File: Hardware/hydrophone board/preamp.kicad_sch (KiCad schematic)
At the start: 10 parts, among them J5 Conn_01x02, U111 AD8541ARTZ

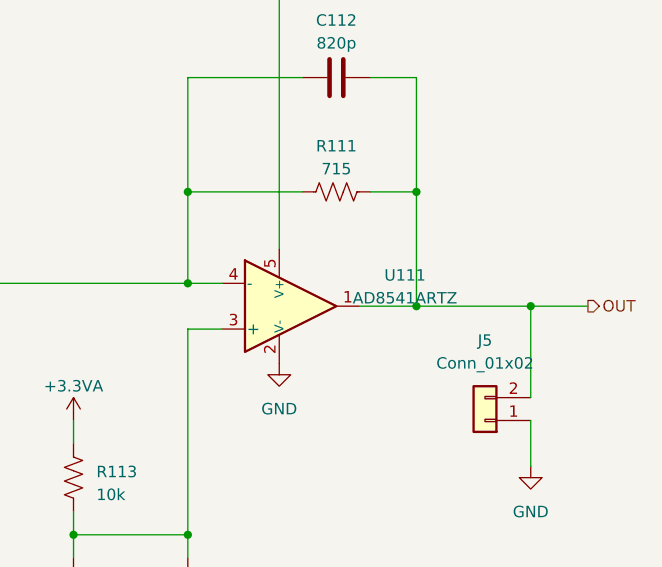
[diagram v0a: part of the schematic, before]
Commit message: changed pre amp op amp
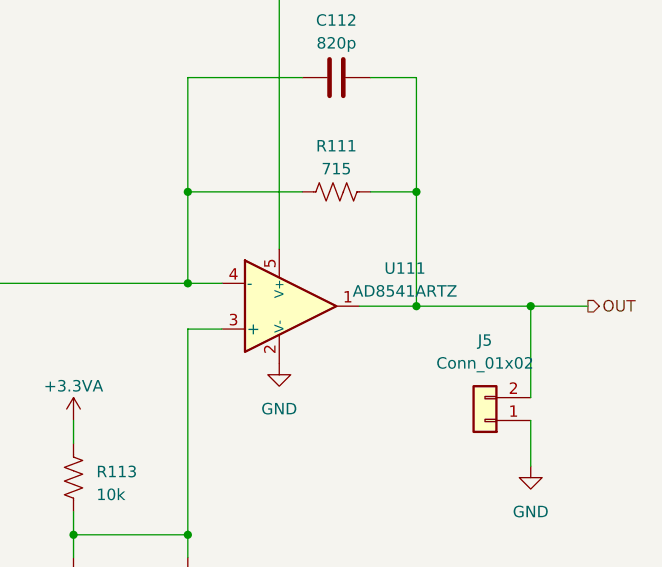
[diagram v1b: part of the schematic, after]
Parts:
- U111: symbol PCM_Amplifier_Operational_AKL:AD8541ARTZ -> PCM_Amplifier_Operational_AKL:AD8628ARTZ
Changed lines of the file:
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@@
     )
   )
-  (symbol (lib_id "PCM_Amplifier_Operational_AKL:AD8541ARTZ") (at 119.38 88.9 0) (unit 1)
+  (symbol (lib_id "PCM_Amplifier_Operational_AKL:AD8628ARTZ") (at 119.38 88.9 0) (unit 1)
     (in_bom yes) (on_board yes) (dnp no) (fields_autoplaced)
-    (property "Reference" "U111" (at 132.08 85.4711 0)
+    (property "Reference" "U111" (at 132.08 84.7091 0)
       (effects (font (size 1.27 1.27)))
     )
-    (property "Value" "AD8541ARTZ" (at 132.08 88.0111 0)
+    (property "Value" "AD8541ARTZ" (at 132.08 87.2491 0)
       (effects (font (size 1.27 1.27)))
     )
@@
       (effects (font (size 1.27 1.27)) hide)
     )
-    (property "Datasheet" "https://www.tme.eu/Document/12dfd4edba370bc858a85650113d6156/AD8541_8542_8544.pdf" (at 119.38 88.9 0)
+    (property "Datasheet" "https://www.tme.eu/Document/4eaf0c682e3035ab5714e0bb38289705/AD8628_8629_8630.pdf" (at 119.38 88.9 0)
       (effects (font (size 1.27 1.27)) hide)
     )
